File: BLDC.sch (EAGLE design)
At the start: 130 parts, among them J1 J_1X4, J2 J_1X6, J3 J_1X7, Q1 IRFS7530TRLPBF, Q2 IRFS7530TRLPBF, Q3 IRFS7530TRLPBF, Q4 IRFS7530TRLPBF, Q5 IRFS7530TRLPBF, Q6 IRFS7530TRLPBF, U1 DRV8302, U102 LM3671MF-3.3/NOPB, U104 MCP2562, U2 STM32F405RGT6, U3 LT3433, Y1 8MHz

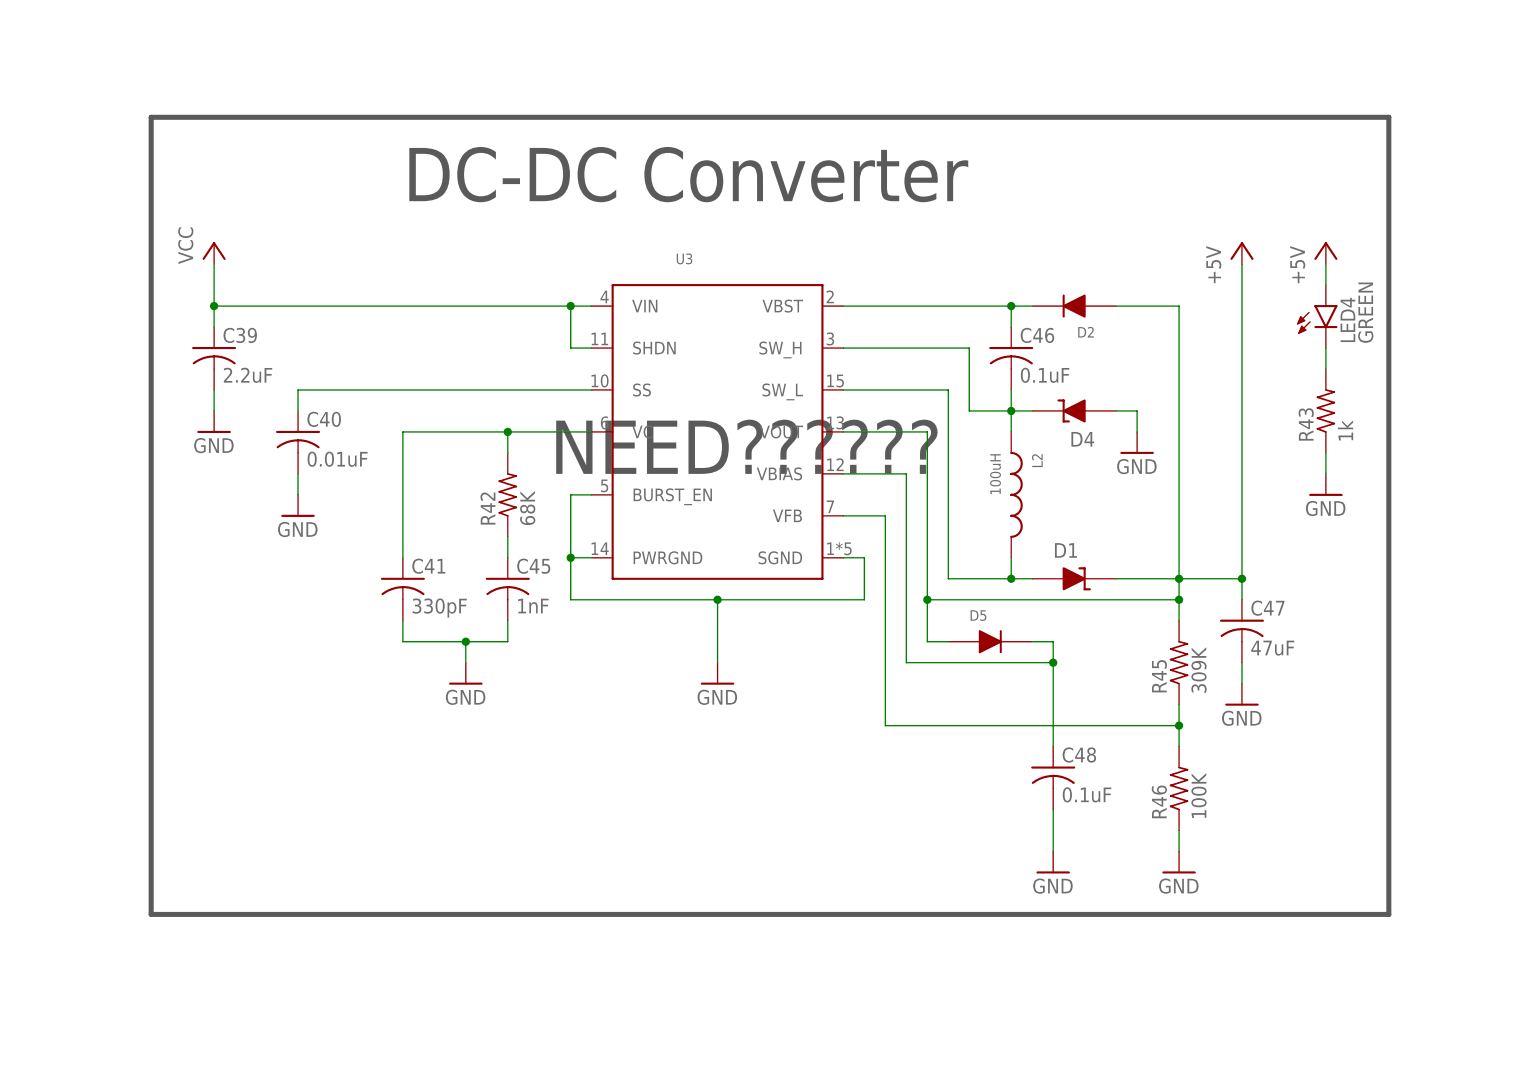
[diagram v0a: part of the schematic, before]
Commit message: Deleted DC-DC Converter
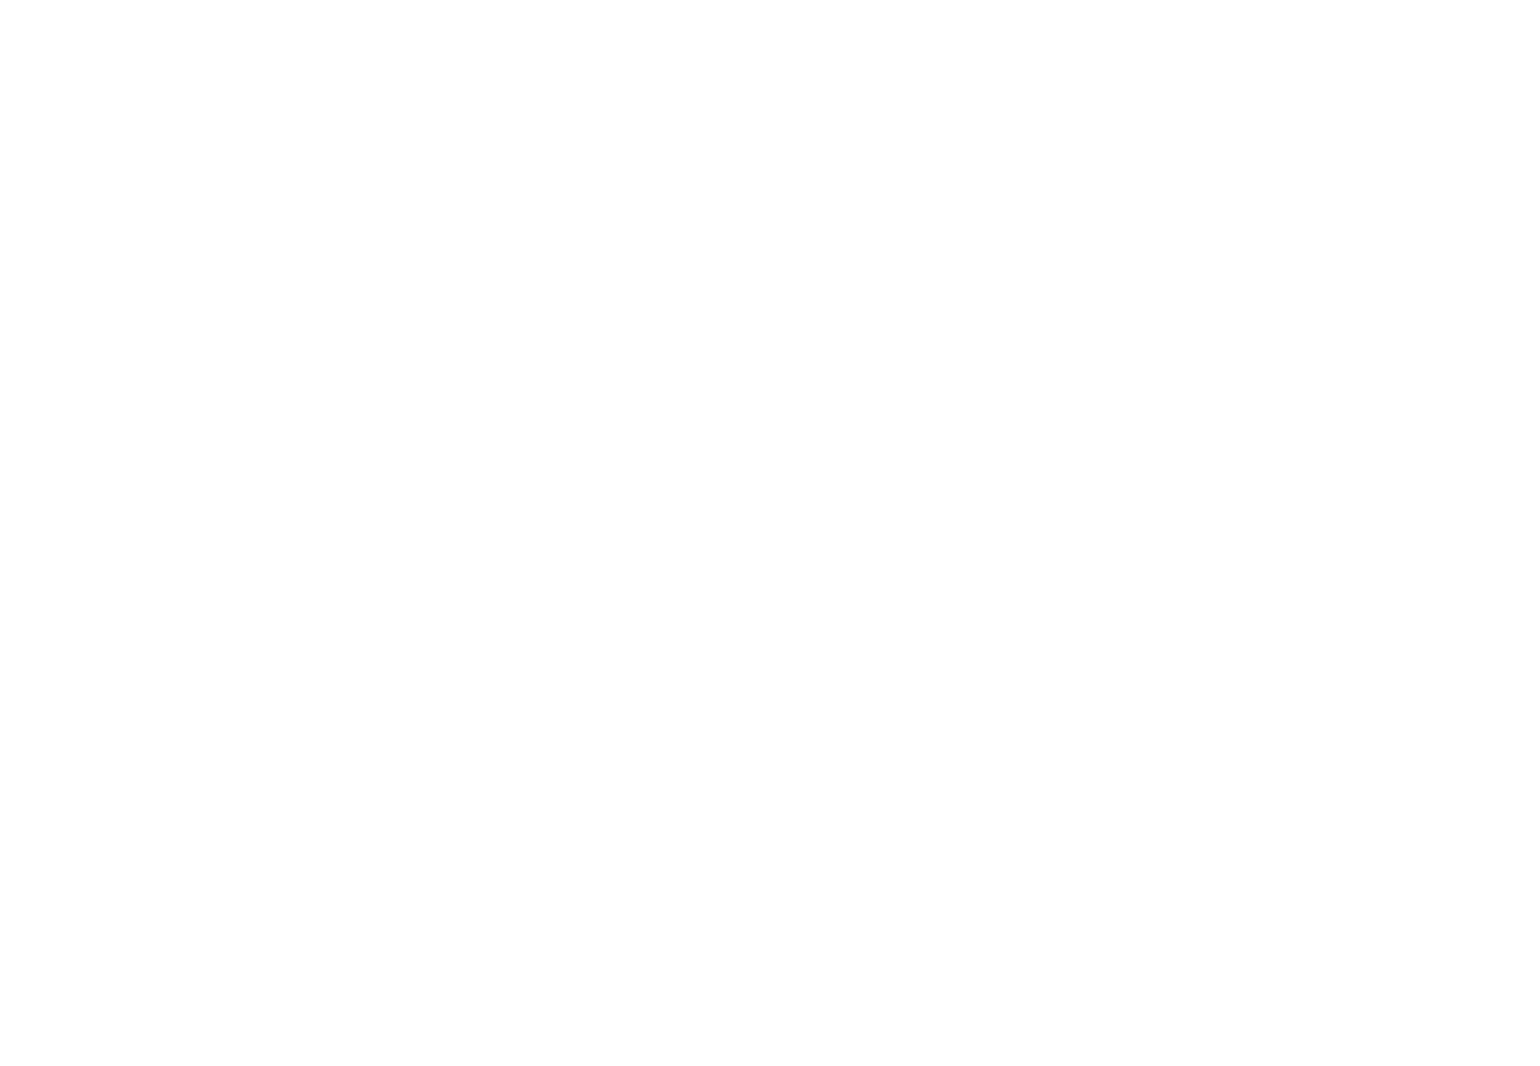
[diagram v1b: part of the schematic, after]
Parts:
- removed C39: 2.2uF, rcl:C-USC0805
- removed C40: 0.01uF, rcl:C-USC0805
- removed C41: 330pF, rcl:C-USC0805
- removed C45: 1nF, rcl:C-USC0805
- removed C46, C48: 0.1uF, rcl:C-USC0805
- removed C47: 47uF, rcl:C-USC0805
- removed D1, D4: 1KSMB160ACT-ND, FormE:1KSMB160ACT-ND
- removed D2, D5: 1N4148WTPMSCT-ND, FormE:1N4148WTPMSCT-ND
- removed L2: 100uH, FormE:L0805
- removed LED4: GREEN, FormE:LEDCHIP-LED0805
- removed R42: 68K, adafruit:R-US_R0805
- removed R43: 1k, adafruit:R-US_R0805
- removed R45: 309K, adafruit:R-US_R0805
- removed R46: 100K, adafruit:R-US_R0805
- removed U3: LT3433, FormE:LT3433
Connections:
- removed net N$36: C48.1, D5.CATHODE, U3.VBIAS
- removed net N$37: D1.ANODE, L2.P$2, U3.SW_L
- removed net N$38: C40.1, U3.SS
- removed net N$39: C45.1, R42.1
- removed net N$40: C41.1, R42.2, U3.VC
- removed net N$41: LED4.C, R43.2
- removed net N$42: C46.1, D2.CATHODE, U3.VBST
- removed net N$43: C46.2, D4.CATHODE, L2.P$1, U3.SW_H
- removed net N$44: R45.1, R46.2, U3.VFB
- net +5V: no longer C47.1, D1.CATHODE, D2.ANODE, D5.ANODE, LED4.A, R45.2, U3.VOUT
- net GND: no longer C39.2, C40.2, C41.2, C45.2, C47.2, C48.2, D4.ANODE, R43.1, R46.1, U3.BURST_EN, U3.PWRGND, U3.SGND
- net VCC: no longer C39.1, U3.SHDN, U3.VIN
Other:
- note removed: "DC-DC Converter"
- note removed: "NEED??????"

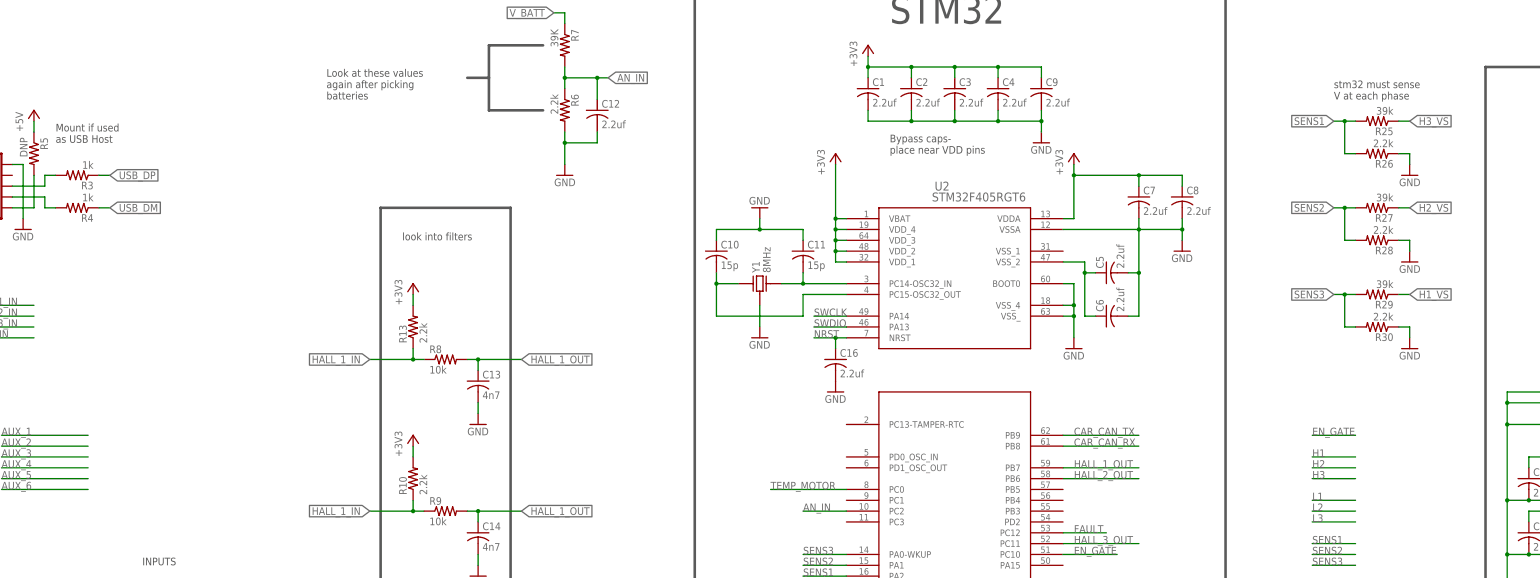
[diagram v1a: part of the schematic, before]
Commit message: coinnected dummy aux
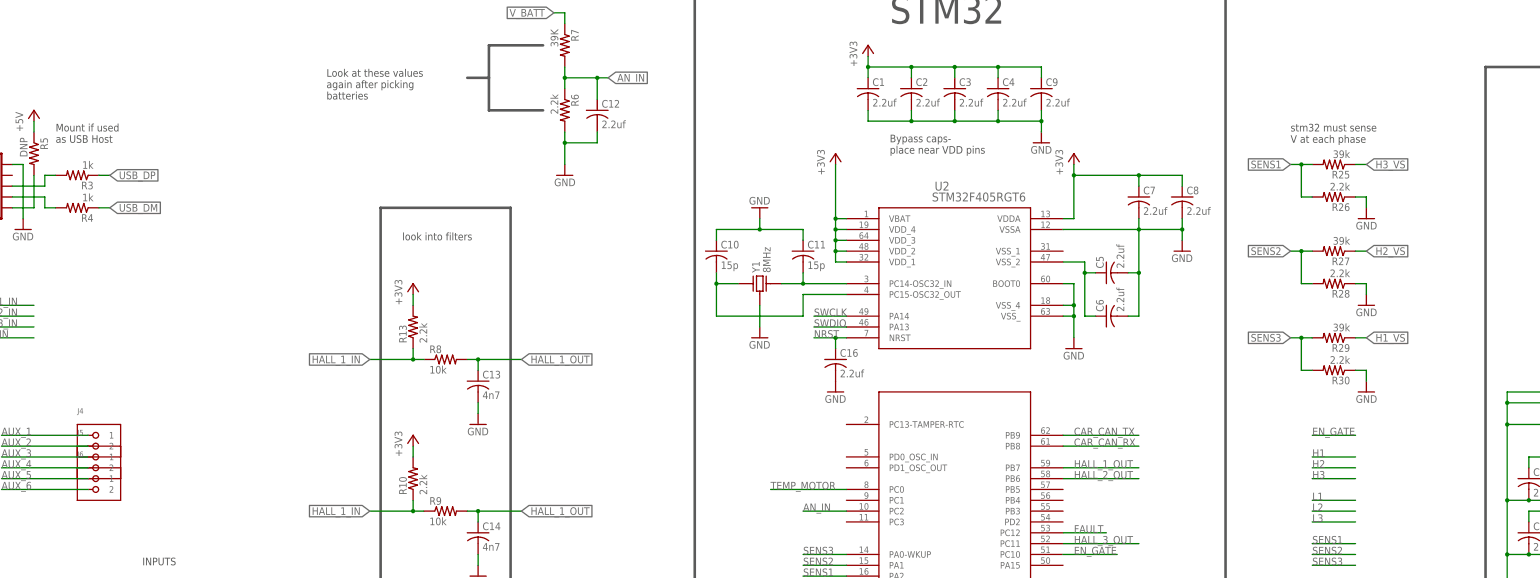
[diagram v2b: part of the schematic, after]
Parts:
- added J4, J5, J6: (no value), FormE:J_1X2
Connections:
- new net AUX_1: J4.1
- new net AUX_2: J4.2
- new net AUX_3: J5.1
- new net AUX_4: J5.2
- new net AUX_5: J6.1
- new net AUX_6: J6.2
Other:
- moved on the sheet: R25, R26, R27, R28, R29, R30

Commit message: org brd modules
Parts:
- added C40: 2200uF, FormE:UVR1J222MHD
- added J7: 1-770178-0, FormE:1-770178-0
- added J8: 1-770174-1, FormE:1-770174-1
- added R42: 10K, FormE:NCP18XH103F03RB
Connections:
- new net DGND: C40.-
- net +3V3: now also J7.5, R42.2
- net ADC_TEMP: now also R42.1
- net GND: now also J7.1
- net NRST: now also J7.2
- net SWCLK: now also J7.4
- net SWDIO: now also J7.3
- net VCC: now also C40.+
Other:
- note added: "60V - 0V V_Batt"
- note removed: "MAKE PART!!!!!!!!!!!!!!!!!!!"
- note removed: "Need big ass cap by v_batt in, maybe 2200uF 63V capacitor?"
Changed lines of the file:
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@@
 <part name="J5" library="FormE" deviceset="J_1X2" device=""/>
 <part name="J6" library="FormE" deviceset="J_1X2" device=""/>
+<part name="J7" library="FormE" deviceset="1-770178-0" device=""/>
+<part name="J8" library="FormE" deviceset="1-770174-1" device=""/>
+<part name="C40" library="FormE" deviceset="UVR1J222MHD" device="" value="2200uF"/>
+<part name="R42" library="FormE" deviceset="NCP18XH103F03RB" device="" value="10K"/>
 </parts>
 <sheets>
@@
 <wire x1="33.02" y1="-48.26" x2="-91.44" y2="-48.26" width="0.6096" layer="97"/>
 <wire x1="-91.44" y1="-48.26" x2="-91.44" y2="139.7" width="0.6096" layer="97"/>
-<text x="-294.64" y="248.92" size="6.4516" layer="97">Need big ass cap by v_batt in, maybe 2200uF 63V capacitor?</text>
 <text x="-256.54" y="157.48" size="1.778" layer="91">Vbatt -&gt; 5V</text>
 <text x="111.76" y="86.36" size="1.778" layer="91">DIODE!!!</text>
@@
 <wire x1="457.2" y1="-10.16" x2="327.66" y2="-10.16" width="0.6096" layer="97"/>
 <wire x1="327.66" y1="-10.16" x2="327.66" y2="63.5" width="0.6096" layer="97"/>
-<text x="-312.42" y="33.02" size="1.778" layer="97">stlinkv2
+<text x="-312.42" y="35.56" size="1.778" layer="97">stlinkv2
 debugger
 connetion</text>
@@
 place only</text>
 <text x="-93.98" y="180.34" size="6.4516" layer="97">NEED TO DECIDE HOW MANY AUX!!!!!!!!!!!!!!</text>
-<text x="-20.32" y="-63.5" size="1.778" layer="97">brd temp</text>
-<text x="-30.48" y="-76.2" size="1.778" layer="97">MAKE PART!!!!!!!!!!!!!!!!!!!</text>
+<text x="-30.48" y="-66.04" size="1.778" layer="97">brd temp</text>
 <text x="347.98" y="-40.64" size="6.4516" layer="97">Need output connect</text>
+<text x="-218.44" y="-30.48" size="1.778" layer="97" rot="R90">60V - 0V V_Batt</text>
 </plain>
 <instances>
@@
 <attribute name="PARTNO" x="139.7" y="-7.62" size="6.4516" layer="96" rot="R270" display="off"/>
 </instance>
-<instance part="P+4" gate="VCC" x="-205.74" y="-12.7" rot="R270"/>
+<instance part="P+4" gate="VCC" x="-210.82" y="-5.08"/>
 <instance part="P+5" gate="VCC" x="205.74" y="73.66"/>
 <instance part="C27" gate="G$1" x="218.44" y="63.5" rot="MR0">
@@
 <instance part="GND17" gate="1" x="111.76" y="-78.74"/>
 <instance part="SUPPLY1" gate="G$1" x="93.98" y="-78.74"/>
-<instance part="SUPPLY2" gate="G$1" x="-205.74" y="-15.24" rot="R90"/>
+<instance part="SUPPLY2" gate="G$1" x="-210.82" y="-30.48"/>
 <instance part="GND37" gate="1" x="-269.24" y="-68.58"/>
 <instance part="P+13" gate="1" x="-269.24" y="-38.1"/>
@@
 <instance part="+3V9" gate="G$1" x="-157.48" y="-38.1"/>
 <instance part="GND43" gate="1" x="-142.24" y="-71.12"/>
-<instance part="+3V10" gate="G$1" x="-20.32" y="-68.58"/>
+<instance part="+3V10" gate="G$1" x="-35.56" y="-68.58"/>
 <instance part="R44" gate="G$1" x="-20.32" y="-88.9" rot="R90">
 <attribute name="PARTNO" x="-20.32" y="-88.9" size="1.778" layer="96" display="off"/>
@@
 <instance part="J5" gate="G$1" x="-226.06" y="25.4"/>
 <instance part="J6" gate="G$1" x="-226.06" y="20.32"/>
+<instance part="J7" gate="G$1" x="-304.8" y="22.86" rot="R180"/>
+<instance part="J8" gate="G$1" x="-327.66" y="-12.7" rot="R180"/>
+<instance part="C40" gate="G$1" x="-213.36" y="-20.32"/>
+<instance part="R42" gate="G$1" x="-27.94" y="-76.2" rot="R180"/>
 </instances>
 <busses>
@@
 <wire x1="-292.1" y1="17.78" x2="-292.1" y2="10.16" width="0.1524" layer="91"/>
 <pinref part="GND26" gate="1" pin="GND"/>
-<wire x1="-292.1" y1="17.78" x2="-297.18" y2="17.78" width="0.1524" layer="91"/>
+<wire x1="-292.1" y1="17.78" x2="-294.64" y2="17.78" width="0.1524" layer="91"/>
+<pinref part="J7" gate="G$1" pin="1"/>
 </segment>
 <segment>
@@
 <wire x1="-292.1" y1="27.94" x2="-292.1" y2="35.56" width="0.1524" layer="91"/>
 <pinref part="+3V7" gate="G$1" pin="+3V3"/>
-<wire x1="-292.1" y1="27.94" x2="-297.18" y2="27.94" width="0.1524" layer="91"/>
+<wire x1="-292.1" y1="27.94" x2="-294.64" y2="27.94" width="0.1524" layer="91"/>
+<pinref part="J7" gate="G$1" pin="5"/>
 </segment>
 <segment>
@@
 <pinref part="+3V9" gate="G$1" pin="+3V3"/>
 <wire x1="-157.48" y1="-40.64" x2="-157.48" y2="-43.18" width="0.1524" layer="91"/>
-</segment>
-<segment>
-<pinref part="+3V10" gate="G$1" pin="+3V3"/>
-<wire x1="-20.32" y1="-71.12" x2="-20.32" y2="-73.66" width="0.1524" layer="91"/>
 </segment>
 <segment>
@@
 <wire x1="-261.62" y1="-48.26" x2="-261.62" y2="-40.64" width="0.1524" layer="91"/>
 <pinref part="+3V11" gate="G$1" pin="+3V3"/>
+</segment>
+<segment>
+<pinref part="R42" gate="G$1" pin="2"/>
+<wire x1="-35.56" y1="-76.2" x2="-35.56" y2="-71.12" width="0.1524" layer="91"/>
+<pinref part="+3V10" gate="G$1" pin="+3V3"/>
 </segment>
 </net>
@@
 <segment>
 <label x="-292.1" y="25.4" size="1.778" layer="95"/>
-<wire x1="-284.48" y1="25.4" x2="-297.18" y2="25.4" width="0.1524" layer="91"/>
+<wire x1="-284.48" y1="25.4" x2="-294.64" y2="25.4" width="0.1524" layer="91"/>
+<pinref part="J7" gate="G$1" pin="4"/>
 </segment>
 </net>
@@
 <segment>
 <label x="-292.1" y="22.86" size="1.778" layer="95"/>
-<wire x1="-284.48" y1="22.86" x2="-297.18" y2="22.86" width="0.1524" layer="91"/>
+<wire x1="-284.48" y1="22.86" x2="-294.64" y2="22.86" width="0.1524" layer="91"/>
+<pinref part="J7" gate="G$1" pin="3"/>
 </segment>
 </net>
@@
 <segment>
 <label x="-292.1" y="20.32" size="1.778" layer="95"/>
-<wire x1="-284.48" y1="20.32" x2="-297.18" y2="20.32" width="0.1524" layer="91"/>
+<wire x1="-284.48" y1="20.32" x2="-294.64" y2="20.32" width="0.1524" layer="91"/>
+<pinref part="J7" gate="G$1" pin="2"/>
 </segment>
 </net>
@@
 </net>
 <net name="VCC" class="0">
-<segment>
-<wire x1="-223.52" y1="-12.7" x2="-208.28" y2="-12.7" width="0.1524" layer="91"/>
-<label x="-223.52" y="-12.7" size="1.778" layer="95"/>
-<pinref part="P+4" gate="VCC" pin="VCC"/>
-</segment>
 <segment>
 <pinref part="U1" gate="G$1" pin="PVDD2"/>
@@
 <wire x1="401.32" y1="43.18" x2="401.32" y2="45.72" width="0.1524" layer="91"/>
 </segment>
+<segment>
+<wire x1="-215.9" y1="-12.7" x2="-213.36" y2="-12.7" width="0.1524" layer="91"/>
+<pinref part="C40" gate="G$1" pin="+"/>
+<wire x1="-213.36" y1="-15.24" x2="-213.36" y2="-12.7" width="0.1524" layer="91"/>
+<pinref part="P+4" gate="VCC" pin="VCC"/>
+<wire x1="-213.36" y1="-12.7" x2="-210.82" y2="-12.7" width="0.1524" layer="91"/>
+<wire x1="-210.82" y1="-12.7" x2="-210.82" y2="-7.62" width="0.1524" layer="91"/>
+<junction x="-213.36" y="-12.7"/>
+</segment>
 </net>
 <net name="N$20" class="0">
@@
 </segment>
 <segment>
-<wire x1="-223.52" y1="-15.24" x2="-208.28" y2="-15.24" width="0.1524" layer="91"/>
-<label x="-223.52" y="-15.24" size="1.778" layer="95"/>
 <pinref part="SUPPLY2" gate="G$1" pin="DGND"/>
+<wire x1="-215.9" y1="-25.4" x2="-213.36" y2="-25.4" width="0.1524" layer="91"/>
+<wire x1="-213.36" y1="-25.4" x2="-210.82" y2="-25.4" width="0.1524" layer="91"/>
+<wire x1="-210.82" y1="-25.4" x2="-210.82" y2="-27.94" width="0.1524" layer="91"/>
+<pinref part="C40" gate="G$1" pin="-"/>
+<wire x1="-213.36" y1="-22.86" x2="-213.36" y2="-25.4" width="0.1524" layer="91"/>
+<junction x="-213.36" y="-25.4"/>
 </segment>
 </net>
@@
 <segment>
 <pinref part="R44" gate="G$1" pin="2"/>
-<wire x1="-20.32" y1="-76.2" x2="-20.32" y2="-81.28" width="0.1524" layer="91"/>
 <pinref part="C50" gate="G$1" pin="1"/>
 <wire x1="-20.32" y1="-81.28" x2="-20.32" y2="-83.82" width="0.1524" layer="91"/>
@@
 <wire x1="-20.32" y1="-81.28" x2="-17.78" y2="-81.28" width="0.1524" layer="91"/>
 <label x="-17.78" y="-81.28" size="1.778" layer="95" xref="yes"/>
-</segment>
-</net>
+<pinref part="R42" gate="G$1" pin="1"/>
+<wire x1="-20.32" y1="-76.2" x2="-20.32" y2="-81.28" width="0.1524" layer="91"/>
+</segment>
+</net>
